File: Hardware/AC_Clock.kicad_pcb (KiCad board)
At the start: 2 copper layers, 132.1 x 100.3 mm, 71 parts, among them J1 L, J2 N, J3 Conn_01x10, J4 Conn_01x10, J5 Conn_01x10, J6 Conn_01x10, SW1 Min_PB, SW2 Hr_PB, T1 10:1, U1 AZ1117-5.0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

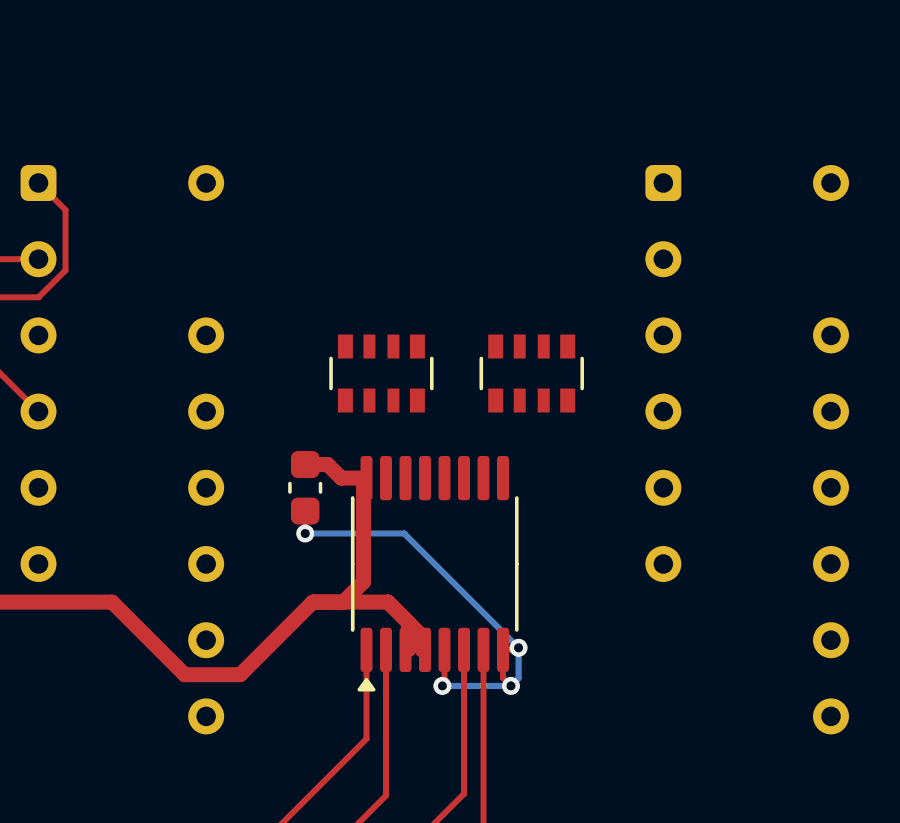
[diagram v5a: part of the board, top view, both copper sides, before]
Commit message: Wire up the 10/Minutes display
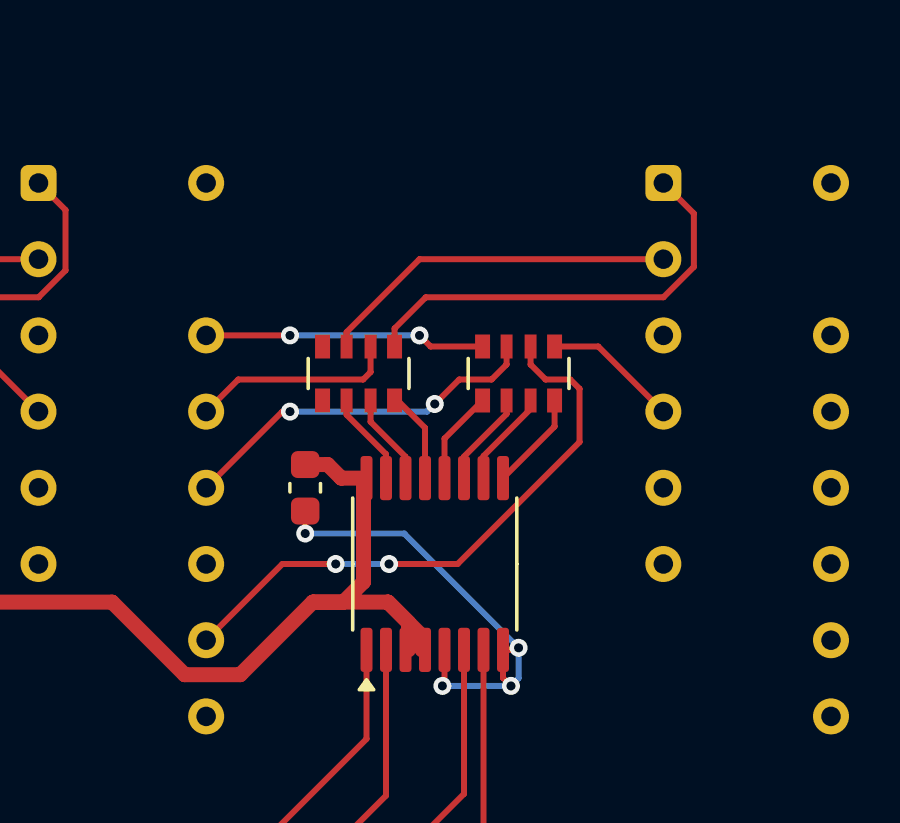
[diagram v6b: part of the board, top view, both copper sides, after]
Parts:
- moved RN3 5.77 mm to (108.2, 61.0)
- moved RN4 4.57 mm to (113.5, 61.0)
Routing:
- net Net-(RN4-R3.2): track 0.00 -> 19.5 mm, vias 0 -> 2
- net Net-(RN3D-R4.2): track 0.00 -> 14.6 mm
- net Net-(RN4-R2.2): track 0.00 -> 12.3 mm, vias 0 -> 2
- net Net-(RN3B-R2.2): track 0.00 -> 12.0 mm
- net Net-(RN4-R1.2): track 0.00 -> 9.37 mm, vias 0 -> 2
- net Net-(RN3C-R3.2): track 0.00 -> 6.88 mm
- net Net-(RN4-R4.2): track 0.00 -> 4.52 mm
- net Net-(RN4-R4.1): track 0.00 -> 3.30 mm
- net Net-(RN4-R3.1): track 0.00 -> 3.24 mm
- net Net-(RN4-R2.1): track 0.00 -> 3.18 mm
- net Net-(RN3B-R2.1): track 0.00 -> 3.13 mm
- net Net-(RN4-R1.1): track 0.00 -> 3.11 mm
- net Net-(RN3C-R3.1): track 0.00 -> 3.07 mm
- net Net-(RN3D-R4.1): track 0.00 -> 3.07 mm

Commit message: Wire up the Hours connectors
Signed-off-by: Joel Cranmer <42.joel.cranmer@gmail.com>
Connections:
- J4 pad 1: unconnected-(J4-Pin_1-Pad1) -> +5V
- J4 pad 10: unconnected-(J4-Pin_10-Pad10) -> DA_4
- J4 pad 2: unconnected-(J4-Pin_2-Pad2) -> GND
- J4 pad 3: unconnected-(J4-Pin_3-Pad3) -> DB_3
- J4 pad 4: unconnected-(J4-Pin_4-Pad4) -> DC_3
- J4 pad 5: unconnected-(J4-Pin_5-Pad5) -> DD_3
- J4 pad 6: unconnected-(J4-Pin_6-Pad6) -> DA_3
- J4 pad 7: unconnected-(J4-Pin_7-Pad7) -> DB_4
- J4 pad 8: unconnected-(J4-Pin_8-Pad8) -> DC_4
- J4 pad 9: unconnected-(J4-Pin_9-Pad9) -> DD_4
- J6 pad 1: unconnected-(J6-Pin_1-Pad1) -> +5V
- J6 pad 10: unconnected-(J6-Pin_10-Pad10) -> DA_4
- J6 pad 2: unconnected-(J6-Pin_2-Pad2) -> GND
- J6 pad 3: unconnected-(J6-Pin_3-Pad3) -> DB_3
- J6 pad 4: unconnected-(J6-Pin_4-Pad4) -> DC_3
- J6 pad 5: unconnected-(J6-Pin_5-Pad5) -> DD_3
- J6 pad 6: unconnected-(J6-Pin_6-Pad6) -> DA_3
- J6 pad 7: unconnected-(J6-Pin_7-Pad7) -> DB_4
- J6 pad 8: unconnected-(J6-Pin_8-Pad8) -> DC_4
- J6 pad 9: unconnected-(J6-Pin_9-Pad9) -> DD_4

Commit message: Fix resistor arrays for more logical layout
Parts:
- renumbered RN6 to RN5, RN5 to RN6, RN8 to RN7, RN7 to RN8
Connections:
- RN5 pad 1: Net-(RN6-R1.1) -> unconnected-(RN5A-R1.1-Pad1)
- RN5 pad 4: unconnected-(RN6-R4.1-Pad4) -> Net-(RN5D-R4.1)
- RN5 pad 5: unconnected-(RN6-R4.2-Pad5) -> Net-(RN5D-R4.2)
- RN5 pad 8: Net-(RN6-R1.2) -> unconnected-(RN5A-R1.2-Pad8)
- RN6 pad 1: Net-(RN5-R1.1) -> Net-(RN6-R1.1)
- RN6 pad 2: Net-(RN5-R2.1) -> Net-(RN6-R2.1)
- RN6 pad 3: Net-(RN5-R3.1) -> Net-(RN6-R3.1)
- RN6 pad 4: Net-(RN5-R4.1) -> Net-(RN6-R4.1)
- RN6 pad 5: Net-(RN5-R4.2) -> Net-(RN6-R4.2)
- RN6 pad 6: Net-(RN5-R3.2) -> Net-(RN6-R3.2)
- RN6 pad 7: Net-(RN5-R2.2) -> Net-(RN6-R2.2)
- RN6 pad 8: Net-(RN5-R1.2) -> Net-(RN6-R1.2)
- RN7 pad 1: Net-(RN8-R1.1) -> unconnected-(RN7A-R1.1-Pad1)
- RN7 pad 2: Net-(RN8-R2.1) -> unconnected-(RN7B-R2.1-Pad2)
- RN7 pad 4: unconnected-(RN8-R4.1-Pad4) -> Net-(RN7D-R4.1)
- RN7 pad 5: unconnected-(RN8-R4.2-Pad5) -> Net-(RN7D-R4.2)
- RN7 pad 8: Net-(RN8-R1.2) -> unconnected-(RN7A-R1.2-Pad8)
- RN8 pad 1: Net-(RN7-R1.1) -> Net-(RN8-R1.1)
- RN8 pad 2: Net-(RN7-R2.1) -> Net-(RN8-R2.1)
- RN8 pad 3: Net-(RN7-R3.1) -> Net-(RN8-R3.1)
- RN8 pad 4: Net-(RN7-R4.1) -> Net-(RN8-R4.1)
- RN8 pad 5: Net-(RN7-R4.2) -> Net-(RN8-R4.2)
- RN8 pad 6: Net-(RN7-R3.2) -> Net-(RN8-R3.2)
- RN8 pad 7: Net-(RN7-R2.2) -> Net-(RN8-R2.2)
- RN8 pad 8: Net-(RN7-R1.2) -> Net-(RN8-R1.2)
- U10 pad 10: Net-(RN5-R4.1) -> Net-(RN6-R3.1)
- U10 pad 11: Net-(RN5-R3.1) -> Net-(RN6-R2.1)
- U10 pad 12: Net-(RN5-R2.1) -> Net-(RN6-R1.1)
- U10 pad 13: Net-(RN5-R1.1) -> Net-(RN5D-R4.1)
- U10 pad 9: Net-(RN6-R1.1) -> Net-(RN6-R4.1)
- U11 pad 1: Net-(RN5-R1.2) -> Net-(RN5D-R4.2)
- U11 pad 10: Net-(RN5-R4.2) -> Net-(RN6-R3.2)
- U11 pad 12: Net-(RN5-R3.2) -> Net-(RN6-R2.2)
- U11 pad 14: Net-(RN5-R2.2) -> Net-(RN6-R1.2)
- U11 pad 4: Net-(RN6-R1.2) -> Net-(RN6-R4.2)
- U12 pad 10: Net-(RN7-R4.1) -> Net-(RN8-R3.1)
- U12 pad 11: Net-(RN7-R3.1) -> Net-(RN8-R2.1)
- U12 pad 12: Net-(RN7-R2.1) -> Net-(RN8-R1.1)
- U12 pad 13: Net-(RN7-R1.1) -> Net-(RN7D-R4.1)
- U12 pad 15: Net-(RN8-R2.1) -> unconnected-(U12-Qf-Pad15)
- U12 pad 9: Net-(RN8-R1.1) -> Net-(RN8-R4.1)
- U13 pad 1: Net-(RN7-R1.2) -> Net-(RN7D-R4.2)
- U13 pad 10: Net-(RN7-R4.2) -> Net-(RN8-R3.2)
- U13 pad 12: Net-(RN7-R3.2) -> Net-(RN8-R2.2)
- U13 pad 14: Net-(RN7-R2.2) -> Net-(RN8-R1.2)
- U13 pad 4: Net-(RN8-R1.2) -> Net-(RN8-R4.2)
